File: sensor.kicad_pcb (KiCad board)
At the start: 2 copper layers, 42.3 x 42.3 mm, 14 parts, among them J1 Conn_01x06_Female, U2 TLV70019_SOT23-5, U3 TXB0106PWR, U4 PMW3360DM-T2QU

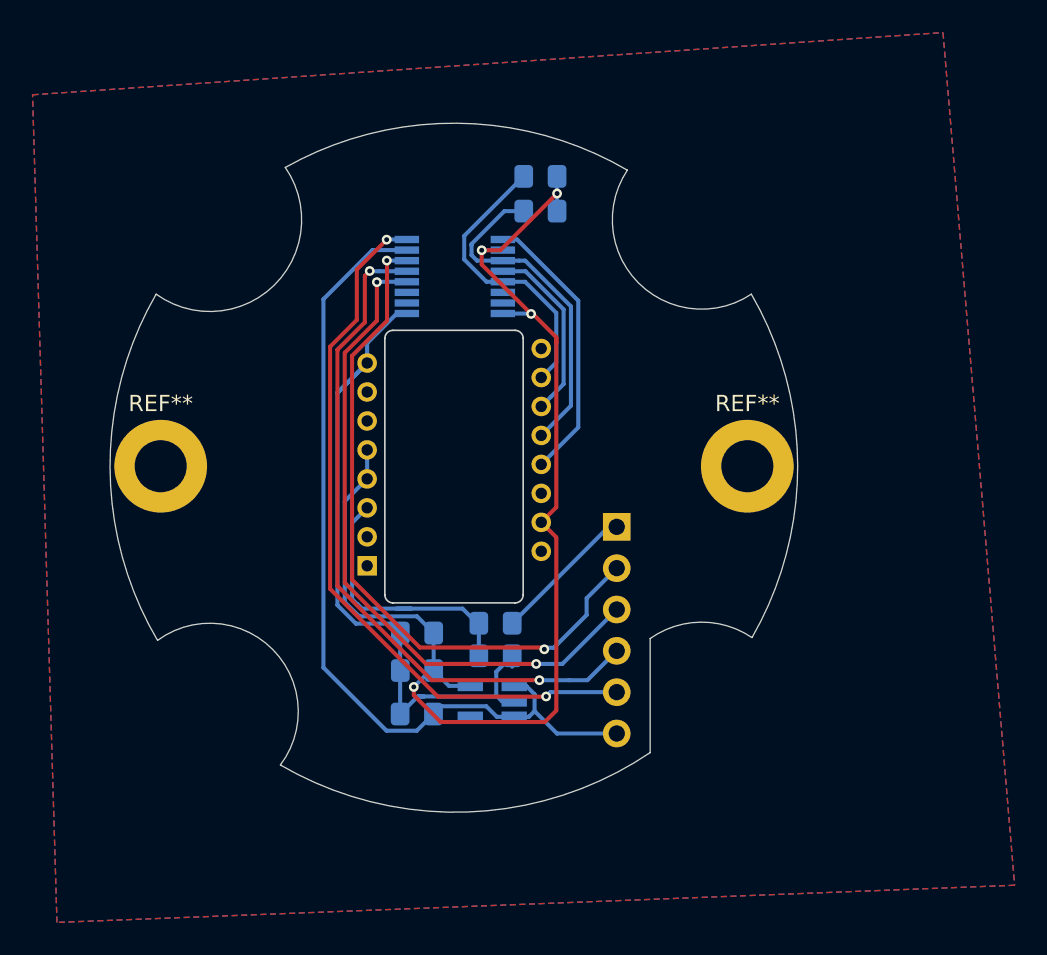
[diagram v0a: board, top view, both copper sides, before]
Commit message: add detrompeur
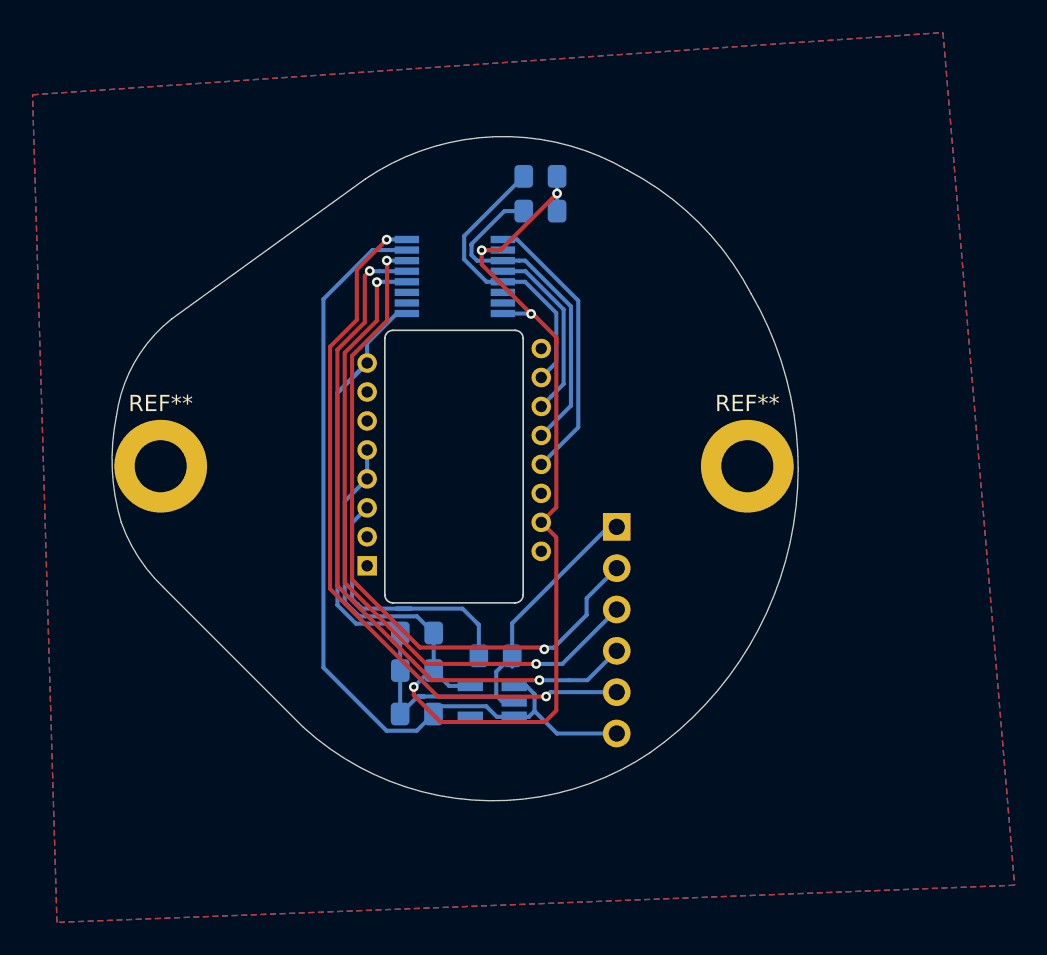
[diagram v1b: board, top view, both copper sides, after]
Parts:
- removed C3: 0.1uF, local:C_0805_2012Metric_Pad1.15x1.40mm_HandSolder
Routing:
- net GND: track 52.6 -> 54.6 mm
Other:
- board size 42.3 x 42.3 mm -> 42.2 x 40.8 mm
- board text added: "rev 1.21"
- board text removed: "rev 1.2"
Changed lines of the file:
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@@
-    )
-  )
-  (footprint "local:C_0805_2012Metric_Pad1.15x1.40mm_HandSolder" (layer "B.Cu")
-    (at 84.1 120.3)
-    (descr "Capacitor SMD 0805 (2012 Metric), square (rectangular) end terminal, IPC_7351 nominal with elongated pad for handsoldering. (Body size source: https://docs.google.com/spreadsheets/d/1BsfQQcO9C6DZCsRaXUlFlo91Tg2WpOkGARC1WS5S8t0/edit?usp=sharing), generated with kicad-footprint-generator")
-    (tags "capacitor handsolder")
-    (property "Sheetfile" "C:/Users/Admin/Documents/GitHub/bastardkb/PMW3360-pcb/sensor.sch")
-    (property "Sheetname" "")
-    (attr smd)
-    (fp_text reference "C3" (at 0 1.65) (layer "B.SilkS") hide
-      (effects (font (size 1 1) (thickness 0.15)) (justify mirror))
-    )
-    (fp_text value "0.1uF" (at 0 -1.65) (layer "B.Fab")
-      (effects (font (size 1 1) (thickness 0.15)) (justify mirror))
-    )
-    (fp_text user "${REFERENCE}" (at 0 0) (layer "B.Fab")
-      (effects (font (size 0.5 0.5) (thickness 0.08)) (justify mirror))
-    )
-    (fp_line (start -0.2 -0.4) (end -0.2 0.4) (layer "B.SilkS") (width 0.12))
-    (fp_line (start 0.2 0.4) (end 0.2 -0.4) (layer "B.SilkS") (width 0.12))
-    (fp_line (start -1.85 -0.95) (end -1.85 0.95) (layer "B.CrtYd") (width 0.05))
-    (fp_line (start 1.85 0.95) (end 1.85 -0.95) (layer "B.CrtYd") (width 0.05))
-    (fp_line (start -1.85 0.95) (end 1.85 0.95) (layer "B.CrtYd") (width 0.05))
-    (fp_line (start 1.85 -0.95) (end -1.85 -0.95) (layer "B.CrtYd") (width 0.05))
-    (fp_line (start -1 0.6) (end 1 0.6) (layer "B.Fab") (width 0.1))
-    (fp_line (start 1 -0.6) (end -1 -0.6) (layer "B.Fab") (width 0.1))
-    (fp_line (start -1 -0.6) (end -1 0.6) (layer "B.Fab") (width 0.1))
-    (fp_line (start 1 0.6) (end 1 -0.6) (layer "B.Fab") (width 0.1))
-    (pad "1" smd roundrect (at -1.025 0) (locked) (size 1.15 1.4) (layers "B.Cu" "B.Paste" "B.Mask") (roundrect_rratio 0.2173913043478261)
-      (net 4 "Net-(C3-Pad1)"))
-    (pad "2" smd roundrect (at 1.025 0) (locked) (size 1.15 1.4) (layers "B.Cu" "B.Paste" "B.Mask") (roundrect_rratio 0.2173913043478261)
-      (net 1 "GND"))
-    (model "${KISYS3DMOD}/Capacitor_SMD.3dshapes/C_0805_2012Metric.wrl"
-      (offset (xyz 0 0 0))
-      (scale (xyz 1 1 1))
-      (rotate (xyz 0 0 0))
     )
   )
@@
     )
   )
+  (gr_circle (center 74.3 116.78725) (end 74.4 116.3) (layer "B.SilkS") (width 0.12) (fill none))
   (gr_arc (start 85.3 118.55) (end 85.3 119.05) (angle -90) (layer "Edge.Cuts") (width 0.1))
-  (gr_arc (start 81.561 110.663) (end 99.822 100.076) (angle 59.99038229) (layer "Edge.Cuts") (width 0.05))
-  (gr_arc (start 96.774 95.504) (end 99.822 100.076) (angle 157.3801351) (layer "Edge.Cuts") (width 0.05))
-  (gr_arc (start 96.774 125.73) (end 99.861875 121.180919) (angle -69.38590141) (layer "Edge.Cuts") (width 0.05))
+  (gr_line (start 76.1 93) (end 64.2 101.6) (layer "Edge.Cuts") (width 0.05))
+  (gr_arc (start 81.36643 110.775725) (end 99.822 100.076) (angle 85.10042958) (layer "Edge.Cuts") (width 0.05))
+  (gr_arc (start 83.908376 108.369623) (end 92.202 92.456) (angle 34.94610302) (layer "Edge.Cuts") (width 0.05))
+  (gr_arc (start 69.905506 108.796453) (end 60.8 107.6) (angle 44.10613232) (layer "Edge.Cuts") (width 0.05))
   (gr_line (start 85.8 102.8) (end 85.8 118.55) (layer "Edge.Cuts") (width 0.1))
   (gr_arc (start 77.8 102.8) (end 77.8 102.3) (angle -90) (layer "Edge.Cuts") (width 0.1))
-  (gr_line (start 93.603338 121.238228) (end 93.603338 128.25) (layer "Edge.Cuts") (width 0.05))
-  (gr_arc (start 81.548631 110.684162) (end 92.202 92.456) (angle -59.70786868) (layer "Edge.Cuts") (width 0.05))
-  (gr_arc (start 81.637359 110.531775) (end 93.603338 128.25) (angle 64.24225617) (layer "Edge.Cuts") (width 0.05))
+  (gr_arc (start 70.775726 110.655778) (end 61.1 114.1) (angle -26.85981358) (layer "Edge.Cuts") (width 0.05))
+  (gr_line (start 72.3 126.7) (end 63.7 118.1) (layer "Edge.Cuts") (width 0.05))
+  (gr_arc (start 84.582269 105.493272) (end 92.202 92.456) (angle -64.47889398) (layer "Edge.Cuts") (width 0.05))
+  (gr_arc (start 83.93671 113.9365) (end 93.603338 128.25) (angle 76.389127) (layer "Edge.Cuts") (width 0.05))
   (gr_arc (start 85.3 102.8) (end 85.8 102.8) (angle -90) (layer "Edge.Cuts") (width 0.1))
   (gr_line (start 77.8 119.05) (end 85.3 119.05) (layer "Edge.Cuts") (width 0.1))
-  (gr_arc (start 81.521862 110.640376) (end 63.246 100.076) (angle -60.52239513) (layer "Edge.Cuts") (width 0.05))
-  (gr_arc (start 66.548 125.73) (end 70.879644 129.008564) (angle -163.4224831) (layer "Edge.Cuts") (width 0.05))
+  (gr_arc (start 73.955093 110.249764) (end 60.8 107.6) (angle -28.06192758) (layer "Edge.Cuts") (width 0.05))
   (gr_line (start 77.8 102.3) (end 85.3 102.3) (layer "Edge.Cuts") (width 0.1))
-  (gr_arc (start 66.548 95.504) (end 63.246 100.076) (angle -160.5688386) (layer "Edge.Cuts") (width 0.05))
   (gr_line (start 77.3 118.55) (end 77.3 102.8) (layer "Edge.Cuts") (width 0.1))
   (gr_arc (start 77.8 118.55) (end 77.3 118.55) (angle -90) (layer "Edge.Cuts") (width 0.1))
@@
     (effects (font (size 0.75 0.75) (thickness 0.1)) (justify mirror))
   )
-  (gr_text "rev 1.2" (at 72.644 109.982 90) (layer "B.SilkS")
+  (gr_text "rev 1.21" (at 72.644 109.982 90) (layer "B.SilkS")
     (effects (font (size 0.75 0.75) (thickness 0.1)) (justify mirror))
   )
@@
   (segment (start 76.211 103.091) (end 76.211 103.459472) (width 0.25) (layer "B.Cu") (net 1))
   (segment (start 78.25 120.9) (end 77.675 120.325) (width 0.25) (layer "B.Cu") (net 1))
+  (segment (start 85.125 122.3) (end 85.125 120.3) (width 0.25) (layer "B.Cu") (net 1))
   (segment (start 84.144989 124.735009) (end 84.50998 125.1) (width 0.25) (layer "B.Cu") (net 1))
   (segment (start 84.079987 124.800011) (end 79.700011 124.800011) (width 0.25) (layer "B.Cu") (net 1))

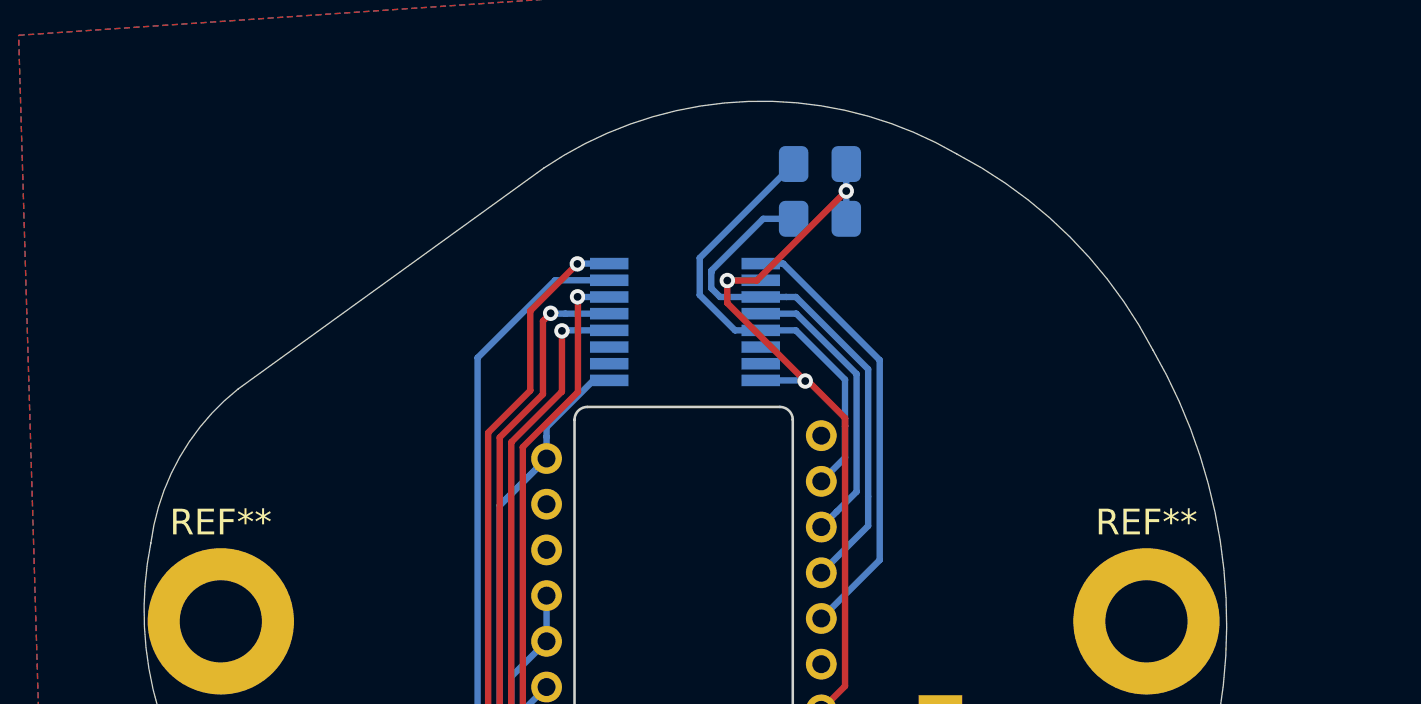
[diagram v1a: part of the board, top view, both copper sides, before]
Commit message: edge cuts and logo
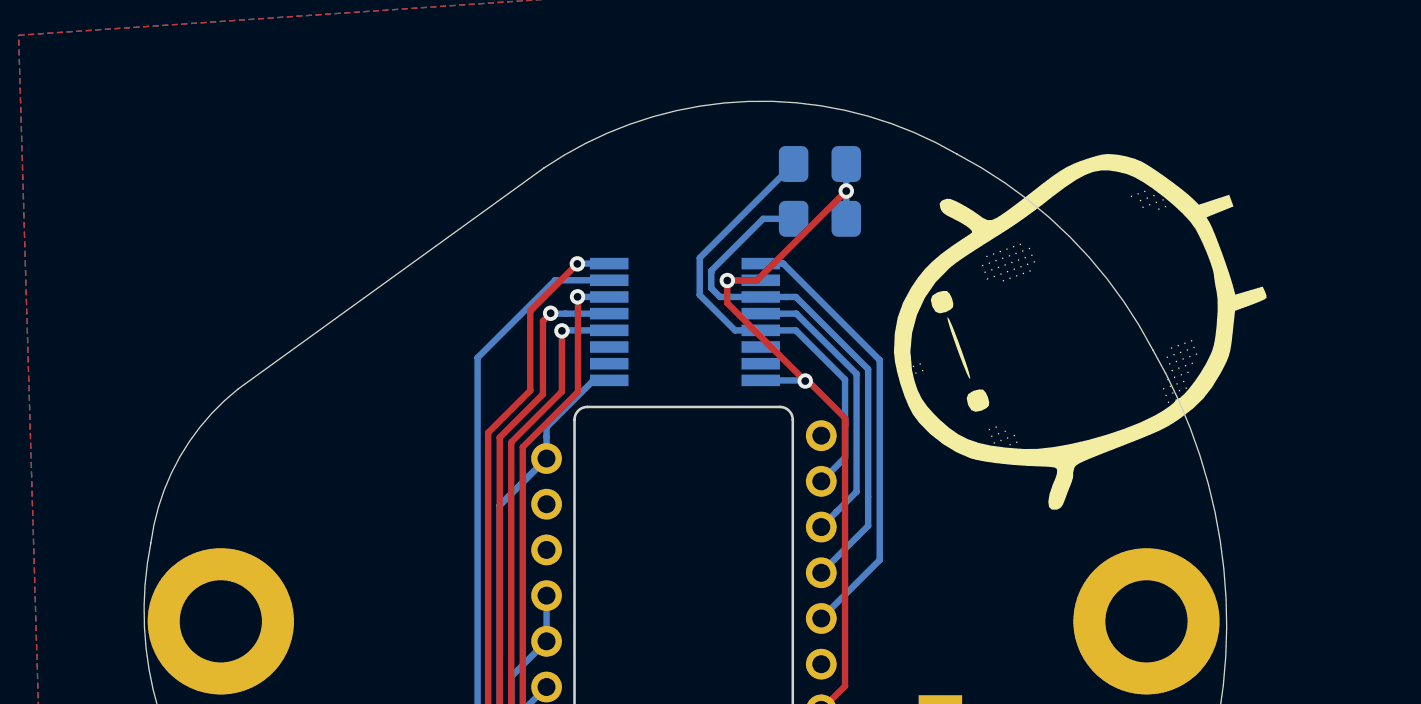
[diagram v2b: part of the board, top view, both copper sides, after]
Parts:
- added G***: LOGO, LOGO, F.Cu at (96.5, 99.9)
